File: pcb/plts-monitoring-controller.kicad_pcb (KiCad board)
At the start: 2 copper layers, 140 x 100 mm, 138 parts, among them J1 GCT USB4105-GF-A, K1 HF115F-1/5V-H, M1 LM2596HVS 5V, Q1 S8050, Q2 S8050, Q20 AO3400A, SW1 RESET, SW2 BOOT, U1 ESP32-WROOM-32E, U11 AP2112K-3.3, U12 USBLC6-2SC6, U2 CP2102N-A02-GQFN24, U3 INA219AIDCNR, U4 ACS712ELCTR-30A-T, U5 ACS712ELCTR-30A-T, U6 SHT31-DIS-B2.5KS, U7 DS3231SN#, U8 MAX3485CSA+, U9 SN65HVD230DR

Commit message: pcb: S12 relay-expansion integration + R1/R2 e-stop fixes (schematic + board)
- 09_EMERGENCY: R1 fix (active-LOW drive: R72 high-side from +3V3, OPT1 cathode
  -> RELAY_CTRL, R78 10k pull-up fail-safe) + R2 fix (inverting sense: Q21
  BSS138 + R77 100k divider + R76 revalued 10k pull-up, C75 filter; HIGH=trip
  matches GPIO14 INPUT_PULLUP contract); truth table/docs updated
- NEW 12_RELAY_EXP: F4 1.1A + FB2 -> +5V_RELAY_EXP rail, J_RELAY_EXP 2x03,
  BSS138 I2C shifters Q22/Q23 + R79/R84 4k7, TVS D24/D25 DNP, INT divider
  R82/R83 (PCF8574 module external, 0x20, active-LOW)
- root sch: sheet 12 entry (page 13); plts-custom: +5V_RELAY_EXP symbol
- pro: PWR netclass pattern for +5V_RELAY_EXP
- 01_POWER: C52 22uF->47uF 25V X5R (relay coil dip headroom)
- board: +7 nets, +14 footprints, pad re-netting, placement to 0 structural
  DRC; repaired broken hand-drawn courtyards (M1/U1/K1/J_I2C_EXP) to true
  geometry; U1 antenna keepout respected

ERC: 0 violations (13 sheets). DRC: 0 structural (courtyard/short/keepout/
clearance clean; silk/via/thermal/isolated = post-routing cleanup).
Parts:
- added D24: SMAJ5.0A, D_SMA, F.Cu at (27.0, 64.8)
- added D25: SMAJ5.0A, D_SMA, F.Cu at (34.5, 64.8)
- added F4: 1.1A hold, Fuse_1812_4532Metric, F.Cu at (60.0, 63.3)
- added FB2: 600R@100MHz, L_0805_2012Metric, F.Cu at (54.5, 65.5)
- added J_RELAY_EXP: RELAY EXP 5V/GND/SDA/SCL/INT, PinHeader_2x03_P2.54mm_Vertical, F.Cu at (6.50, 58.0)
- added Q21: BSS138, SOT-23, F.Cu at (15.5, 64.5)
- added Q22: BSS138, SOT-23, F.Cu at (15.0, 53.5)
- added Q23: BSS138, SOT-23, F.Cu at (15.0, 60.8)
- added R77: 100k 1%, R_0603_1608Metric, F.Cu at (20.5, 64.5)
- added R78: 10k 1%, R_0603_1608Metric, F.Cu at (47.7, 64.5)
- added R79: 4.7k 1%, R_0603_1608Metric, F.Cu at (14.6, 49.8)
- added R82: 10k 1%, R_0603_1608Metric, F.Cu at (11.0, 61.5)
- added R83: 15k 1%, R_0603_1608Metric, F.Cu at (40.0, 64.8)
- added R84: 4.7k 1%, R_0603_1608Metric, F.Cu at (11.0, 63.5)
- C52: value 22uF 25V X7R -> 47uF 25V X5R
- moved R87 1.49 mm to (55.5, 70.8)
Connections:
- OPT1 pad 2: DGND -> RELAY_CTRL
- R72 pad 1: RELAY_CTRL -> +3V3
- R75 pad 2: E_STOP_SENSE -> Net-(Q21-G)
- R76 pad 2: DGND -> +3V3

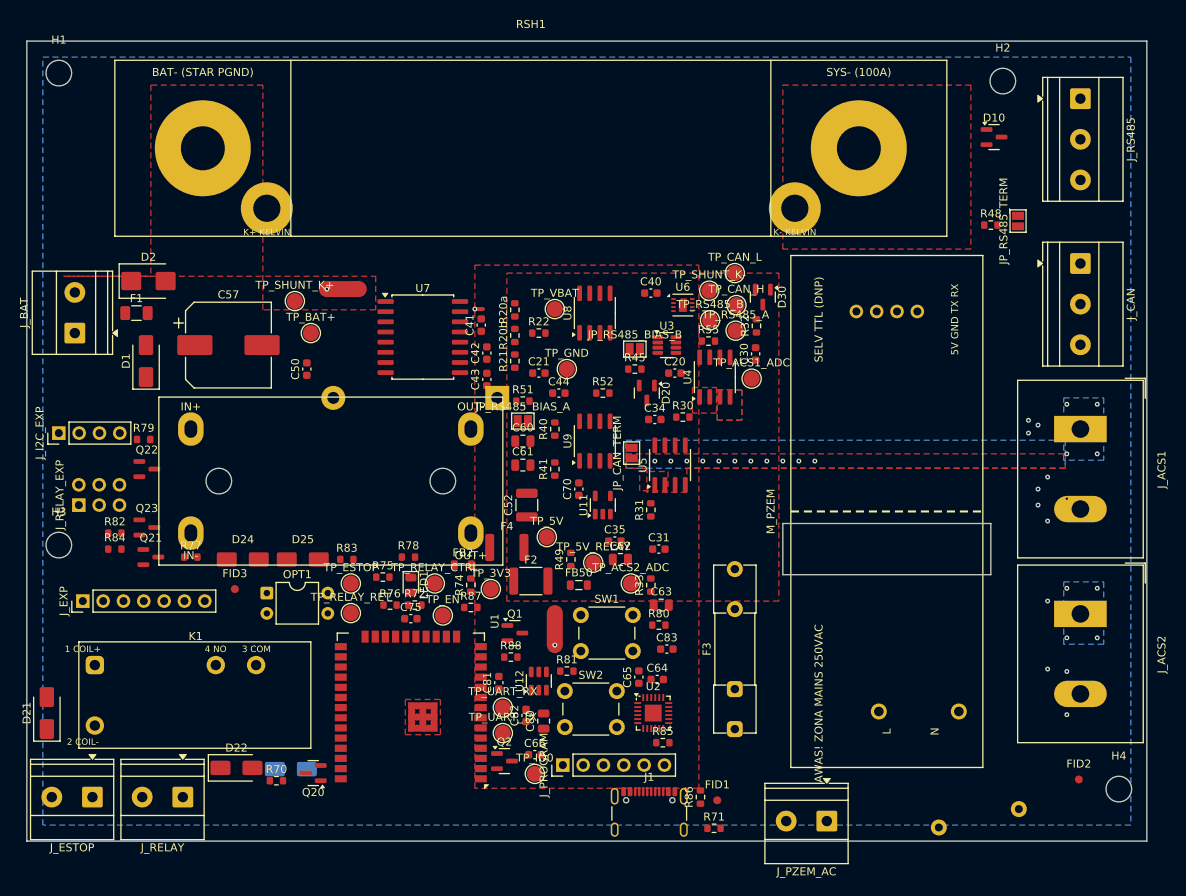
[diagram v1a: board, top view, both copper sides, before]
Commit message: pcb: route S12 board (Freerouting API + A* bridges) + S10 fab outputs + docs
- Full board routing via Freerouting 2.1.0 REST API (SSE snapshots) with
  iterative import/export cycles, plus deterministic A* bridge router
  (escape-cell validation, via grid, string-pull smoothing, selective
  ripup-reroute with no-rip heal cycles)
- Ground architecture: PGND B.Cu pour + NT0/NT1/NT2 star-ties preserved
  (added NT2 PGND tie-down via); pour fragmentation bridged; collinear
  track merge (4394 -> ~1850 segments)
- DRC: 0 errors / 157 warnings (silk cosmetic + starved thermals with
  routed connectivity); 13 unconnected pairs documented (mains creepage
  corridor needs interactive push-and-shove; 11 fragment leftovers)
- Critical nets verified connected: E_STOP_SENSE, RELAY_CTRL, GPIO33,
  RS485_TX, I2C, CAN, PZEM, L_AC_FUSED (post-check exact clearance)
- NT net-tie keepouts refined to tracks-only over exposed bridges
- S10: 9-layer gerbers + Excellon PTH/NPTH + PickAndPlace (pcb/fab/)
- docs: BOM, HARDWARE_REVISION (routing recap section 9), TEST_PLAN,
  README_DESIGN, PickAndPlace
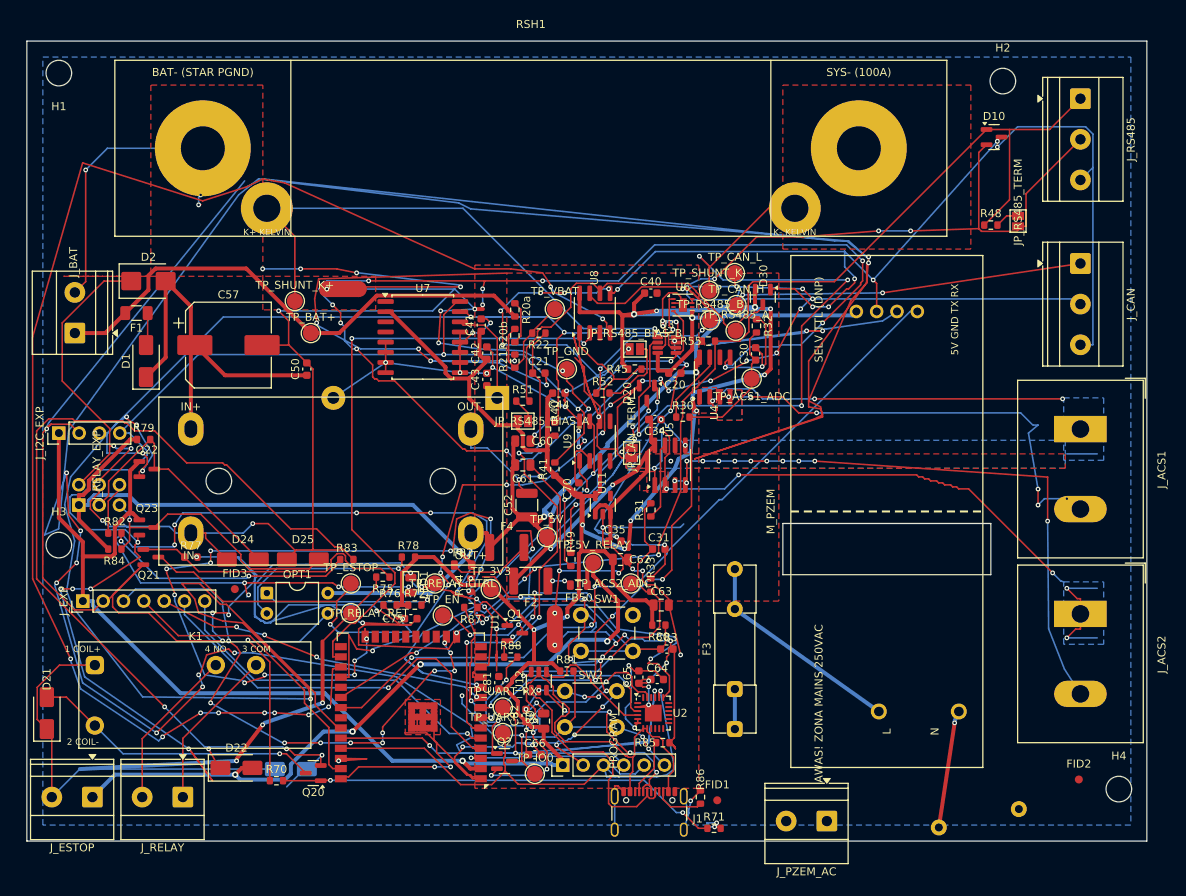
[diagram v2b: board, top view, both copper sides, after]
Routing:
- net DGND: track 0.00 -> 771.6 mm, vias 1 -> 67
- net UART0_RX: track 0.00 -> 479.8 mm, vias 0 -> 13
- net PGND: track 0.00 -> 413.1 mm, vias 2 -> 27
- net +3V3: track 0.00 -> 396.3 mm, vias 0 -> 14
- net AGND: track 0.00 -> 319.4 mm, vias 0 -> 27
- net I2C_SDA: track 0.00 -> 241.4 mm, vias 0 -> 8
- net I2C_SCL: track 0.00 -> 188.2 mm, vias 0 -> 9
- net RS485_TX: track 0.00 -> 178.3 mm, vias 0 -> 10
- net +5V: track 0.00 -> 163.5 mm, vias 0 -> 5
- net CAN_L: track 0.00 -> 149.4 mm, vias 0 -> 12
- net RS485_B: track 0.00 -> 113.4 mm, vias 0 -> 6
- net RS485_A: track 0.00 -> 112.7 mm
- net Net-(LED1-A): track 0.00 -> 105.5 mm, vias 0 -> 9
- net RELAY_RET: track 0.00 -> 103.1 mm, vias 0 -> 3
- net PZEM_TX: track 0.00 -> 95.9 mm, vias 0 -> 3
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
